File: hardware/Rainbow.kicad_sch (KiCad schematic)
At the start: 22 parts, among them J1 PICKit3, J2 UART, J3 BARREL_JACK, J4 HC-05, J5 RGB, Q1 Q_NMOS_GDS, Q2 Q_NMOS_GDS, Q3 Q_NMOS_GDS, SW1 SWITCH, U1 PIC16F15325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

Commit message: Finish wiring
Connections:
- net VDC: now also J5.1, J5.2; no longer J5.7, J5.8
- net at J5.5, J5.6: now also Q2.2 (D); no longer Q1.2 (D)
- net at J5.3, J5.4: now also Q3.2 (D); no longer Q2.2 (D)
- new net: J5.7, J5.8, Q1.2 (D)
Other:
- moved on the sheet: J5
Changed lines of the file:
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@@
   (junction (at 101.6 138.43) (diameter 0) (color 0 0 0 0)
   )
+  (junction (at 189.23 82.55) (diameter 0) (color 0 0 0 0)
+  )
   (junction (at 162.56 140.97) (diameter 0) (color 0 0 0 0)
   )
@@
   (junction (at 142.24 58.42) (diameter 0) (color 0 0 0 0)
   )
+  (junction (at 189.23 97.79) (diameter 0) (color 0 0 0 0)
+  )
   (junction (at 177.8 140.97) (diameter 0) (color 0 0 0 0)
   )
@@
   (junction (at 177.8 135.89) (diameter 0) (color 0 0 0 0)
   )
-  (junction (at 184.15 82.55) (diameter 0) (color 0 0 0 0)
-  )
-  (junction (at 184.15 97.79) (diameter 0) (color 0 0 0 0)
-  )
-  (junction (at 184.15 87.63) (diameter 0) (color 0 0 0 0)
+  (junction (at 189.23 87.63) (diameter 0) (color 0 0 0 0)
+  )
+  (junction (at 189.23 92.71) (diameter 0) (color 0 0 0 0)
   )
   (junction (at 82.55 143.51) (diameter 0) (color 0 0 0 0)
-  )
-  (junction (at 184.15 92.71) (diameter 0) (color 0 0 0 0)
   )
   (no_connect (at 67.31 101.6))
@@
     (stroke (width 0) (type default) (color 0 0 0 0))
   )
-  (wire (pts (xy 184.15 96.52) (xy 184.15 97.79))
-    (stroke (width 0) (type default) (color 0 0 0 0))
-  )
-  (wire (pts (xy 176.53 97.79) (xy 184.15 97.79))
+  (wire (pts (xy 189.23 96.52) (xy 189.23 97.79))
     (stroke (width 0) (type default) (color 0 0 0 0))
   )
@@
     (stroke (width 0) (type default) (color 0 0 0 0))
   )
+  (wire (pts (xy 189.23 97.79) (xy 189.23 99.06))
+    (stroke (width 0) (type default) (color 0 0 0 0))
+  )
   (wire (pts (xy 129.54 135.89) (xy 129.54 137.16))
     (stroke (width 0) (type default) (color 0 0 0 0))
@@
     (stroke (width 0) (type default) (color 0 0 0 0))
   )
-  (wire (pts (xy 184.15 82.55) (xy 184.15 83.82))
+  (wire (pts (xy 189.23 81.28) (xy 189.23 82.55))
     (stroke (width 0) (type default) (color 0 0 0 0))
   )
@@
     (stroke (width 0) (type default) (color 0 0 0 0))
   )
-  (wire (pts (xy 184.15 92.71) (xy 184.15 93.98))
+  (wire (pts (xy 189.23 91.44) (xy 189.23 92.71))
     (stroke (width 0) (type default) (color 0 0 0 0))
   )
@@
     (stroke (width 0) (type default) (color 0 0 0 0))
   )
-  (wire (pts (xy 179.07 77.47) (xy 179.07 82.55))
+  (wire (pts (xy 184.15 77.47) (xy 184.15 97.79))
+    (stroke (width 0) (type default) (color 0 0 0 0))
+  )
+  (wire (pts (xy 184.15 97.79) (xy 189.23 97.79))
     (stroke (width 0) (type default) (color 0 0 0 0))
   )
@@
     (stroke (width 0) (type default) (color 0 0 0 0))
   )
-  (wire (pts (xy 166.37 93.98) (xy 166.37 92.71))
-    (stroke (width 0) (type default) (color 0 0 0 0))
-  )
   (wire (pts (xy 134.62 66.04) (xy 134.62 69.85))
     (stroke (width 0) (type default) (color 0 0 0 0))
   )
-  (wire (pts (xy 156.21 85.09) (xy 156.21 83.82))
+  (wire (pts (xy 156.21 82.55) (xy 156.21 85.09))
     (stroke (width 0) (type default) (color 0 0 0 0))
   )
@@
     (stroke (width 0) (type default) (color 0 0 0 0))
   )
+  (wire (pts (xy 189.23 87.63) (xy 189.23 88.9))
+    (stroke (width 0) (type default) (color 0 0 0 0))
+  )
+  (wire (pts (xy 166.37 87.63) (xy 166.37 93.98))
+    (stroke (width 0) (type default) (color 0 0 0 0))
+  )
   (wire (pts (xy 134.62 58.42) (xy 142.24 58.42))
     (stroke (width 0) (type default) (color 0 0 0 0))
@@
     (stroke (width 0) (type default) (color 0 0 0 0))
   )
-  (wire (pts (xy 156.21 83.82) (xy 176.53 83.82))
-    (stroke (width 0) (type default) (color 0 0 0 0))
-  )
   (wire (pts (xy 101.6 144.78) (xy 101.6 138.43))
     (stroke (width 0) (type default) (color 0 0 0 0))
@@
     (stroke (width 0) (type default) (color 0 0 0 0))
   )
-  (wire (pts (xy 184.15 97.79) (xy 184.15 99.06))
-    (stroke (width 0) (type default) (color 0 0 0 0))
-  )
-  (wire (pts (xy 176.53 83.82) (xy 176.53 87.63))
-    (stroke (width 0) (type default) (color 0 0 0 0))
-  )
   (wire (pts (xy 176.53 113.03) (xy 176.53 116.84))
     (stroke (width 0) (type default) (color 0 0 0 0))
@@
     (stroke (width 0) (type default) (color 0 0 0 0))
   )
+  (wire (pts (xy 176.53 92.71) (xy 189.23 92.71))
+    (stroke (width 0) (type default) (color 0 0 0 0))
+  )
   (wire (pts (xy 144.78 107.95) (xy 168.91 107.95))
     (stroke (width 0) (type default) (color 0 0 0 0))
@@
     (stroke (width 0) (type default) (color 0 0 0 0))
   )
-  (wire (pts (xy 179.07 82.55) (xy 184.15 82.55))
-    (stroke (width 0) (type default) (color 0 0 0 0))
-  )
   (wire (pts (xy 134.62 60.96) (xy 134.62 58.42))
     (stroke (width 0) (type default) (color 0 0 0 0))
@@
     (stroke (width 0) (type default) (color 0 0 0 0))
   )
-  (wire (pts (xy 184.15 86.36) (xy 184.15 87.63))
+  (wire (pts (xy 189.23 86.36) (xy 189.23 87.63))
     (stroke (width 0) (type default) (color 0 0 0 0))
   )
@@
     (stroke (width 0) (type default) (color 0 0 0 0))
   )
+  (wire (pts (xy 189.23 82.55) (xy 189.23 83.82))
+    (stroke (width 0) (type default) (color 0 0 0 0))
+  )
   (wire (pts (xy 115.57 109.22) (xy 115.57 115.57))
     (stroke (width 0) (type default) (color 0 0 0 0))
@@
     (stroke (width 0) (type default) (color 0 0 0 0))
   )
-  (wire (pts (xy 176.53 102.87) (xy 176.53 97.79))
+  (wire (pts (xy 176.53 92.71) (xy 176.53 102.87))
     (stroke (width 0) (type default) (color 0 0 0 0))
   )
@@
     (stroke (width 0) (type default) (color 0 0 0 0))
   )
-  (wire (pts (xy 176.53 87.63) (xy 184.15 87.63))
-    (stroke (width 0) (type default) (color 0 0 0 0))
-  )
   (wire (pts (xy 77.47 63.5) (xy 77.47 72.39))
     (stroke (width 0) (type default) (color 0 0 0 0))
@@
     (stroke (width 0) (type default) (color 0 0 0 0))
   )
+  (wire (pts (xy 156.21 82.55) (xy 189.23 82.55))
+    (stroke (width 0) (type default) (color 0 0 0 0))
+  )
   (wire (pts (xy 57.15 104.14) (xy 67.31 104.14))
     (stroke (width 0) (type default) (color 0 0 0 0))
   )
-  (wire (pts (xy 184.15 81.28) (xy 184.15 82.55))
-    (stroke (width 0) (type default) (color 0 0 0 0))
-  )
-  (wire (pts (xy 184.15 91.44) (xy 184.15 92.71))
+  (wire (pts (xy 189.23 92.71) (xy 189.23 93.98))
     (stroke (width 0) (type default) (color 0 0 0 0))
   )
@@
     (stroke (width 0) (type default) (color 0 0 0 0))
   )
-  (wire (pts (xy 166.37 92.71) (xy 184.15 92.71))
-    (stroke (width 0) (type default) (color 0 0 0 0))
-  )
   (wire (pts (xy 115.57 82.55) (xy 115.57 86.36))
     (stroke (width 0) (type default) (color 0 0 0 0))
@@
     (stroke (width 0) (type default) (color 0 0 0 0))
   )
-  (wire (pts (xy 184.15 87.63) (xy 184.15 88.9))
+  (wire (pts (xy 166.37 87.63) (xy 189.23 87.63))
     (stroke (width 0) (type default) (color 0 0 0 0))
   )
@@
     (pin "6")
   )
-  (symbol (lib_id "Rainbow:Wago") (at 194.31 88.9 0) (mirror x) (unit 1)
+  (symbol (lib_id "Rainbow:Wago") (at 199.39 88.9 0) (mirror x) (unit 1)
     (in_bom yes) (on_board yes)
-    (property "Reference" "J5" (id 0) (at 193.04 104.14 0)
+    (property "Reference" "J5" (id 0) (at 198.12 104.14 0)
       (effects (font (size 1.524 1.524)))
     )
-    (property "Value" "RGB" (id 1) (at 193.04 101.6 0)
+    (property "Value" "RGB" (id 1) (at 198.12 101.6 0)
       (effects (font (size 1.524 1.524)))
     )
-    (property "Footprint" "Rainbow:Wago" (id 2) (at 194.31 88.9 0)
+    (property "Footprint" "Rainbow:Wago" (id 2) (at 199.39 88.9 0)
       (effects (font (size 1.27 1.27) italic) hide)
     )
-    (property "Datasheet" "" (id 3) (at 194.31 88.9 0)
+    (property "Datasheet" "" (id 3) (at 199.39 88.9 0)
       (effects (font (size 1.27 1.27) italic) hide)
     )
@@
     (pin "1")
   )
-  (symbol (lib_id "power:VDC") (at 179.07 77.47 0) (unit 1)
+  (symbol (lib_id "power:VDC") (at 184.15 77.47 0) (unit 1)
     (in_bom yes) (on_board yes)
-    (property "Reference" "#PWR014" (id 0) (at 179.07 80.01 0)
-      (effects (font (size 1.27 1.27)) hide)
-    )
-    (property "Value" "VDC" (id 1) (at 179.07 73.66 0))
-    (property "Footprint" "" (id 2) (at 179.07 77.47 0)
-      (effects (font (size 1.27 1.27)) hide)
-    )
-    (property "Datasheet" "" (id 3) (at 179.07 77.47 0)
-      (effects (font (size 1.27 1.27)) hide)
-    )
+    (property "Reference" "#PWR014" (id 0) (at 184.15 80.01 0)
+      (effects (font (size 1.27 1.27)) hide)
+    )
+    (property "Value" "VDC" (id 1) (at 184.15 73.66 0))
+    (property "Footprint" "" (id 2) (at 184.15 77.47 0)
+      (effects (font (size 1.27 1.27)) hide)
+    )
+    (property "Datasheet" "" (id 3) (at 184.15 77.47 0)
+      (effects (font (size 1.27 1.27)) hide)
+    )

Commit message: 0.1 uF bypass capacitor
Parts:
- added C3: 0.1uF, Capacitor_THT:C_Disc_D3.0mm_W1.6mm_P2.50mm, symbol Device:C_Small
- renumbered R4 to R2, R2 to R3, R3 to R4
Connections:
- net +5V: now also C3.1
- net GNDREF: now also C3.2
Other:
- moved on the sheet: C2, D2, R2

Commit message: Change diode footprint
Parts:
- D3: footprint Diode_THT:D_T-1_P5.08mm_Horizontal -> Diode_THT:D_DO-41_SOD81_P7.62mm_Horizontal
- L1: footprint Capacitor_THT:C_Radial_D5.0mm_H7.0mm_P2.00mm -> Capacitor_THT:CP_Radial_Tantal_D4.5mm_P2.50mm
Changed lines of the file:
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@@
     (property "Reference" "L1" (id 0) (at 168.91 138.43 90))
     (property "Value" "100uH" (id 1) (at 168.91 142.24 90))
-    (property "Footprint" "Capacitor_THT:C_Radial_D5.0mm_H7.0mm_P2.00mm" (id 2) (at 168.91 140.97 0)
+    (property "Footprint" "Capacitor_THT:CP_Radial_Tantal_D4.5mm_P2.50mm" (id 2) (at 168.91 140.97 0)
       (effects (font (size 1.27 1.27)) hide)
     )
@@
       (effects (font (size 1.27 1.27)) (justify left) hide)
     )
-    (property "Footprint" "Diode_THT:D_T-1_P5.08mm_Horizontal" (id 2) (at 162.56 146.05 0)
+    (property "Footprint" "Diode_THT:D_DO-41_SOD81_P7.62mm_Horizontal" (id 2) (at 162.56 146.05 0)
       (effects (font (size 1.27 1.27)) hide)
     )
@@
     )
     (path "/a23e0cc4-0850-4f31-bb65-206b872ef2d3"
-      (reference "D3") (unit 1) (value "D_Schottky") (footprint "Diode_THT:D_T-1_P5.08mm_Horizontal")
+      (reference "D3") (unit 1) (value "D_Schottky") (footprint "Diode_THT:D_DO-41_SOD81_P7.62mm_Horizontal")
     )
     (path "/410def68-8b62-4888-9363-5c9e7c3dbfbc"
@@
     )
     (path "/1d6fab55-8b7b-47d1-9cf1-815f63776650"
-      (reference "L1") (unit 1) (value "100uH") (footprint "Capacitor_THT:C_Radial_D5.0mm_H7.0mm_P2.00mm")
+      (reference "L1") (unit 1) (value "100uH") (footprint "Capacitor_THT:CP_Radial_Tantal_D4.5mm_P2.50mm")
     )
     (path "/ae2697a6-5b6c-4144-a80c-f59c20cf01e1"

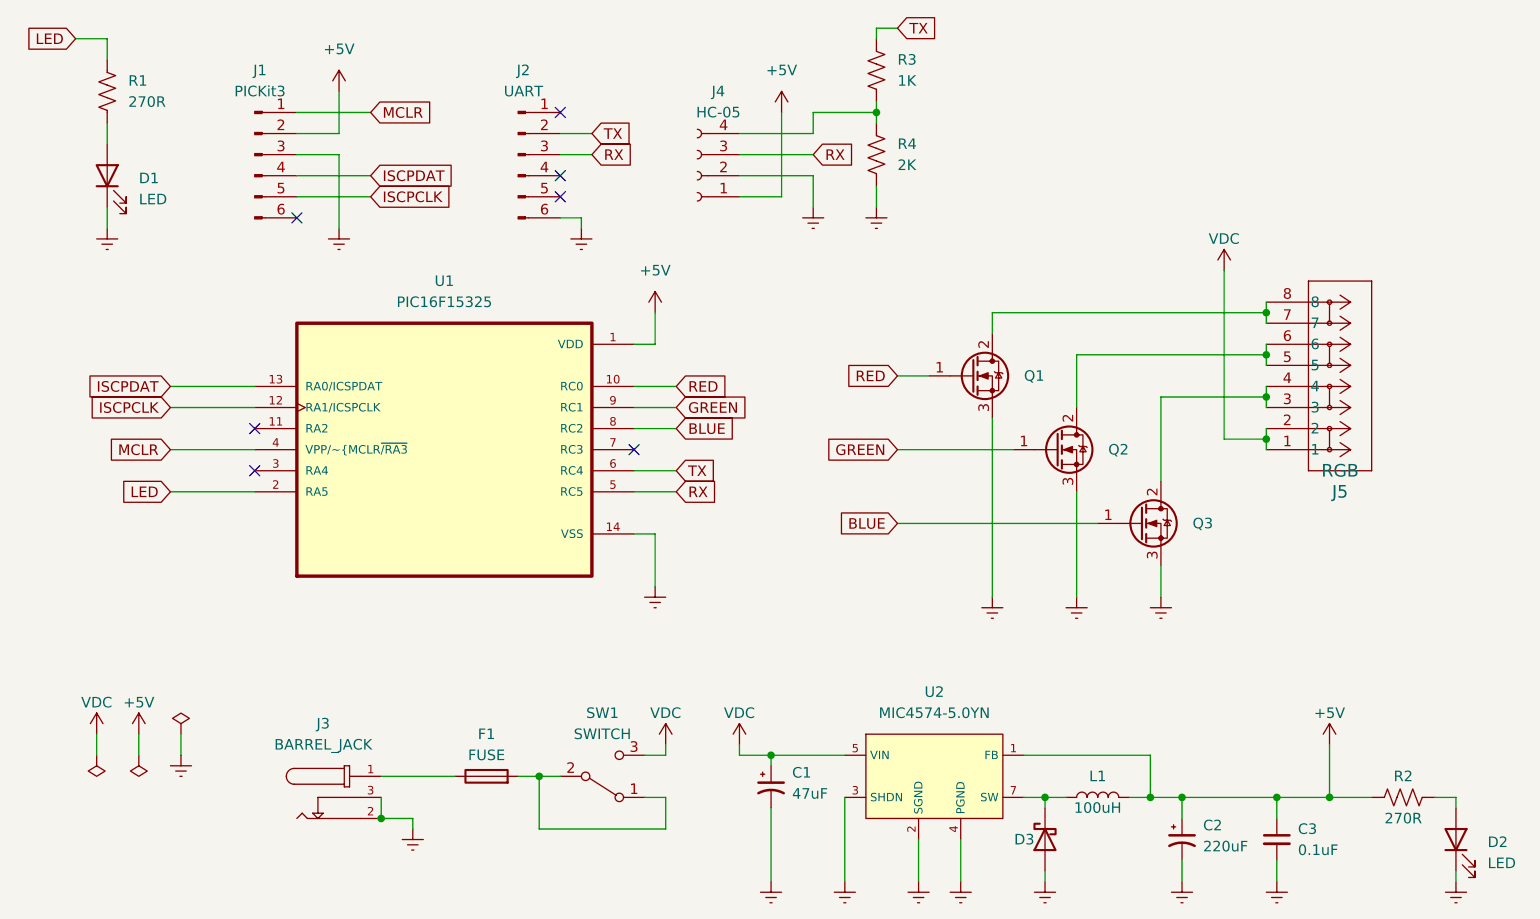
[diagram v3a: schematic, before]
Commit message: Diodes for reverse polarity protection
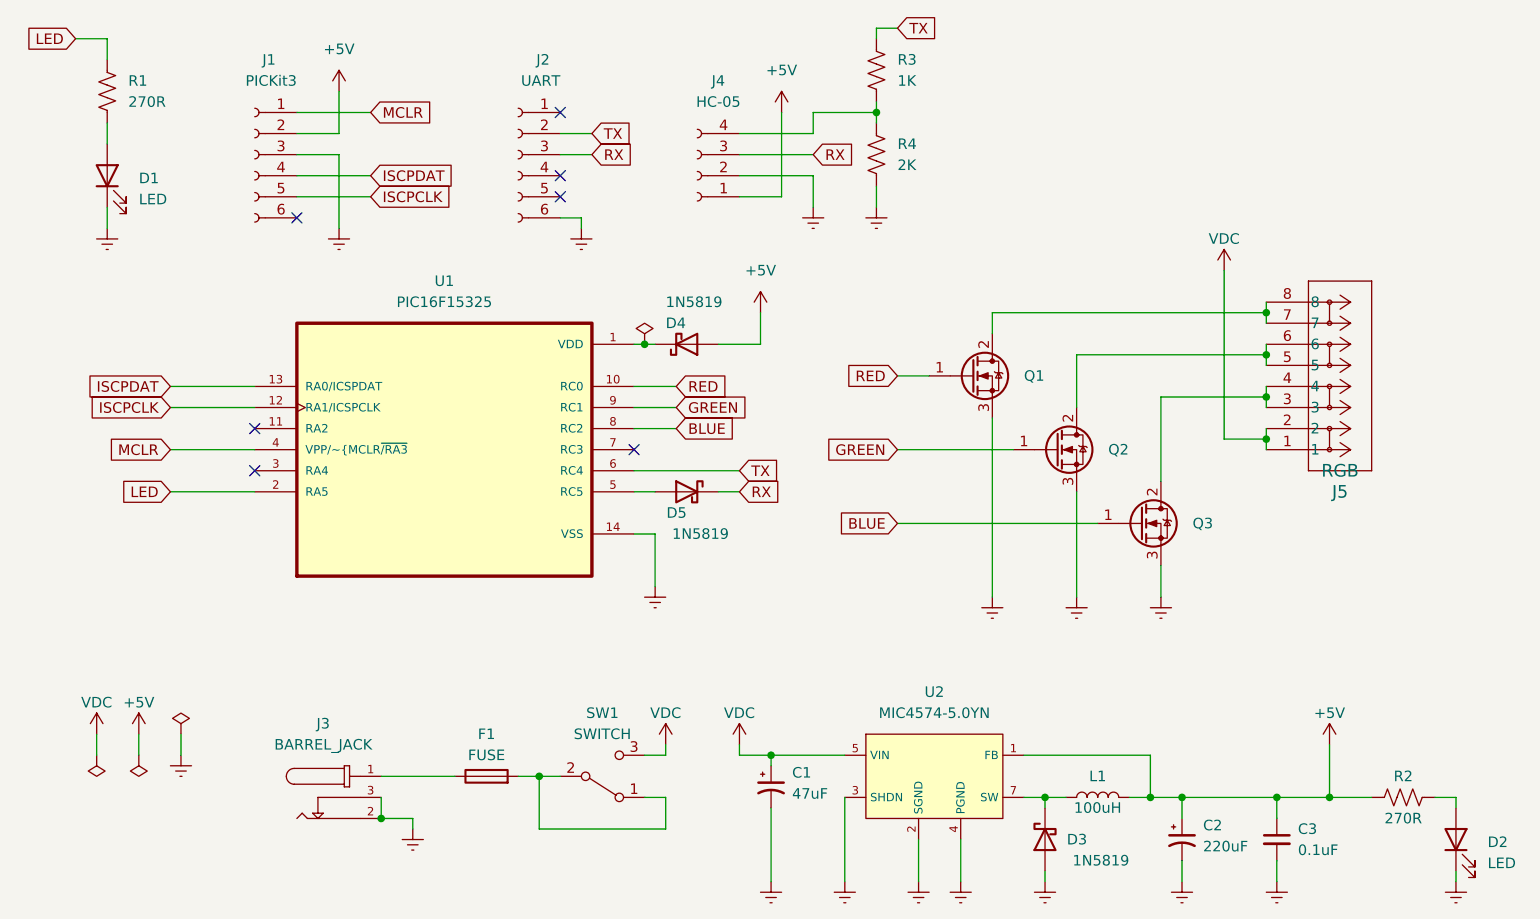
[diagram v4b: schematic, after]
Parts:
- removed J1: PICKit3, Connector_PinHeader_2.54mm:PinHeader_1x06_P2.54mm_Vertical, symbol Connector:Conn_01x06_Male
- removed J2: UART, Connector_PinHeader_2.54mm:PinHeader_1x06_P2.54mm_Vertical, symbol Connector:Conn_01x06_Male
- added D4, D5: 1N5819, Diode_THT:D_DO-41_SOD81_P7.62mm_Horizontal, symbol Device:D_Schottky
- added J1: PICKit3, Connector_PinSocket_2.54mm:PinSocket_1x06_P2.54mm_Vertical, symbol Connector:Conn_01x06_Female
- added J2: UART, Connector_PinSocket_2.54mm:PinSocket_1x06_P2.54mm_Vertical, symbol Connector:Conn_01x06_Female
- D3: value D_Schottky -> 1N5819
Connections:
- net +5V: now also D4.2 (A), J1.2 (Pin_2); no longer U1.1 (VDD)
- net GNDREF: now also J1.3 (Pin_3), J2.6 (Pin_6)
- net ISCPCLK: now also J1.5 (Pin_5)
- net ISCPDAT: now also J1.4 (Pin_4)
- net MCLR: now also J1.1 (Pin_1)
- net RX: now also D5.1 (K), J2.3 (Pin_3); no longer U1.5 (RC5)
- net TX: now also J2.2 (Pin_2)
- new net: D5.2 (A), U1.5 (RC5)
- new net: D4.1 (K), U1.1 (VDD)

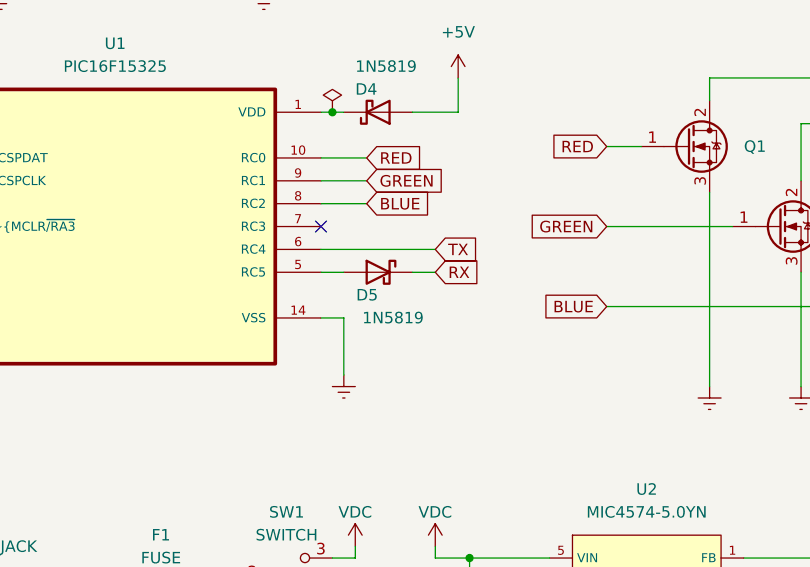
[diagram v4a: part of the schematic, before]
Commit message: Remove extra diode on RX line
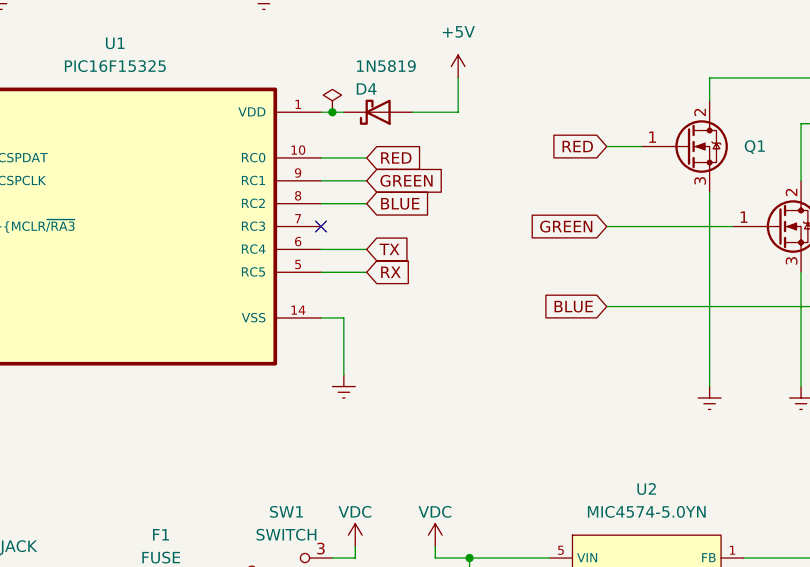
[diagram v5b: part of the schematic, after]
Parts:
- removed D5: 1N5819, Diode_THT:D_DO-41_SOD81_P7.62mm_Horizontal, symbol Device:D_Schottky
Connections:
- net RX: now also U1.5 (RC5)
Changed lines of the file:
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@@
-    (stroke (width 0) (type default) (color 0 0 0 0))
-  )
-  (wire (pts (xy 123.19 104.14) (xy 125.73 104.14))
     (stroke (width 0) (type default) (color 0 0 0 0))
   )
@@
     (stroke (width 0) (type default) (color 0 0 0 0))
   )
-  (wire (pts (xy 113.03 101.6) (xy 125.73 101.6))
+  (wire (pts (xy 113.03 101.6) (xy 118.11 101.6))
     (stroke (width 0) (type default) (color 0 0 0 0))
   )
@@
     (stroke (width 0) (type default) (color 0 0 0 0))
   )
-  (wire (pts (xy 113.03 104.14) (xy 115.57 104.14))
+  (wire (pts (xy 113.03 104.14) (xy 118.11 104.14))
     (stroke (width 0) (type default) (color 0 0 0 0))
   )
@@
     )
   )
-  (global_label "RX" (shape input) (at 125.73 104.14 0) (fields_autoplaced)
+  (global_label "RX" (shape input) (at 118.11 104.14 0) (fields_autoplaced)
     (effects (font (size 1.27 1.27)) (justify left))
-    (property "Intersheet References" "${INTERSHEET_REFS}" (id 0) (at 130.6226 104.0606 0)
+    (property "Intersheet References" "${INTERSHEET_REFS}" (id 0) (at 123.0026 104.0606 0)
       (effects (font (size 1.27 1.27)) (justify left) hide)
     )
@@
     )
   )
-  (global_label "TX" (shape input) (at 125.73 101.6 0) (fields_autoplaced)
+  (global_label "TX" (shape input) (at 118.11 101.6 0) (fields_autoplaced)
     (effects (font (size 1.27 1.27)) (justify left))
-    (property "Intersheet References" "${INTERSHEET_REFS}" (id 0) (at 130.3202 101.5206 0)
+    (property "Intersheet References" "${INTERSHEET_REFS}" (id 0) (at 122.7002 101.5206 0)
       (effects (font (size 1.27 1.27)) (justify left) hide)
     )
@@
     )
     (pin "1")
-  )
-  (symbol (lib_id "Device:D_Schottky") (at 119.38 104.14 0) (mirror y) (unit 1)
-    (in_bom yes) (on_board yes)
-    (property "Reference" "D5" (id 0) (at 119.38 106.68 0)
-      (effects (font (size 1.27 1.27)) (justify left))
-    )
-    (property "Value" "1N5819" (id 1) (at 124.46 109.22 0)
-      (effects (font (size 1.27 1.27)) (justify left))
-    )
-    (property "Footprint" "Diode_THT:D_DO-41_SOD81_P7.62mm_Horizontal" (id 2) (at 119.38 104.14 0)
-      (effects (font (size 1.27 1.27)) hide)
-    )
-    (property "Datasheet" "~" (id 3) (at 119.38 104.14 0)
-      (effects (font (size 1.27 1.27)) hide)
-    )
-    (pin "1")
-    (pin "2")
   )
   (symbol (lib_id "Device:C_Polarized_Small_US") (at 129.54 139.7 0) (unit 1)
@@
       (reference "D4") (unit 1) (value "1N5819") (footprint "Diode_THT:D_DO-41_SOD81_P7.62mm_Horizontal")
     )
-    (path "/02972ebd-2649-44ae-933b-65029a0cf05a"
-      (reference "D5") (unit 1) (value "1N5819") (footprint "Diode_THT:D_DO-41_SOD81_P7.62mm_Horizontal")
-    )
     (path "/410def68-8b62-4888-9363-5c9e7c3dbfbc"
